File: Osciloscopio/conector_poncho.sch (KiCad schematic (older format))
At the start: 1 part

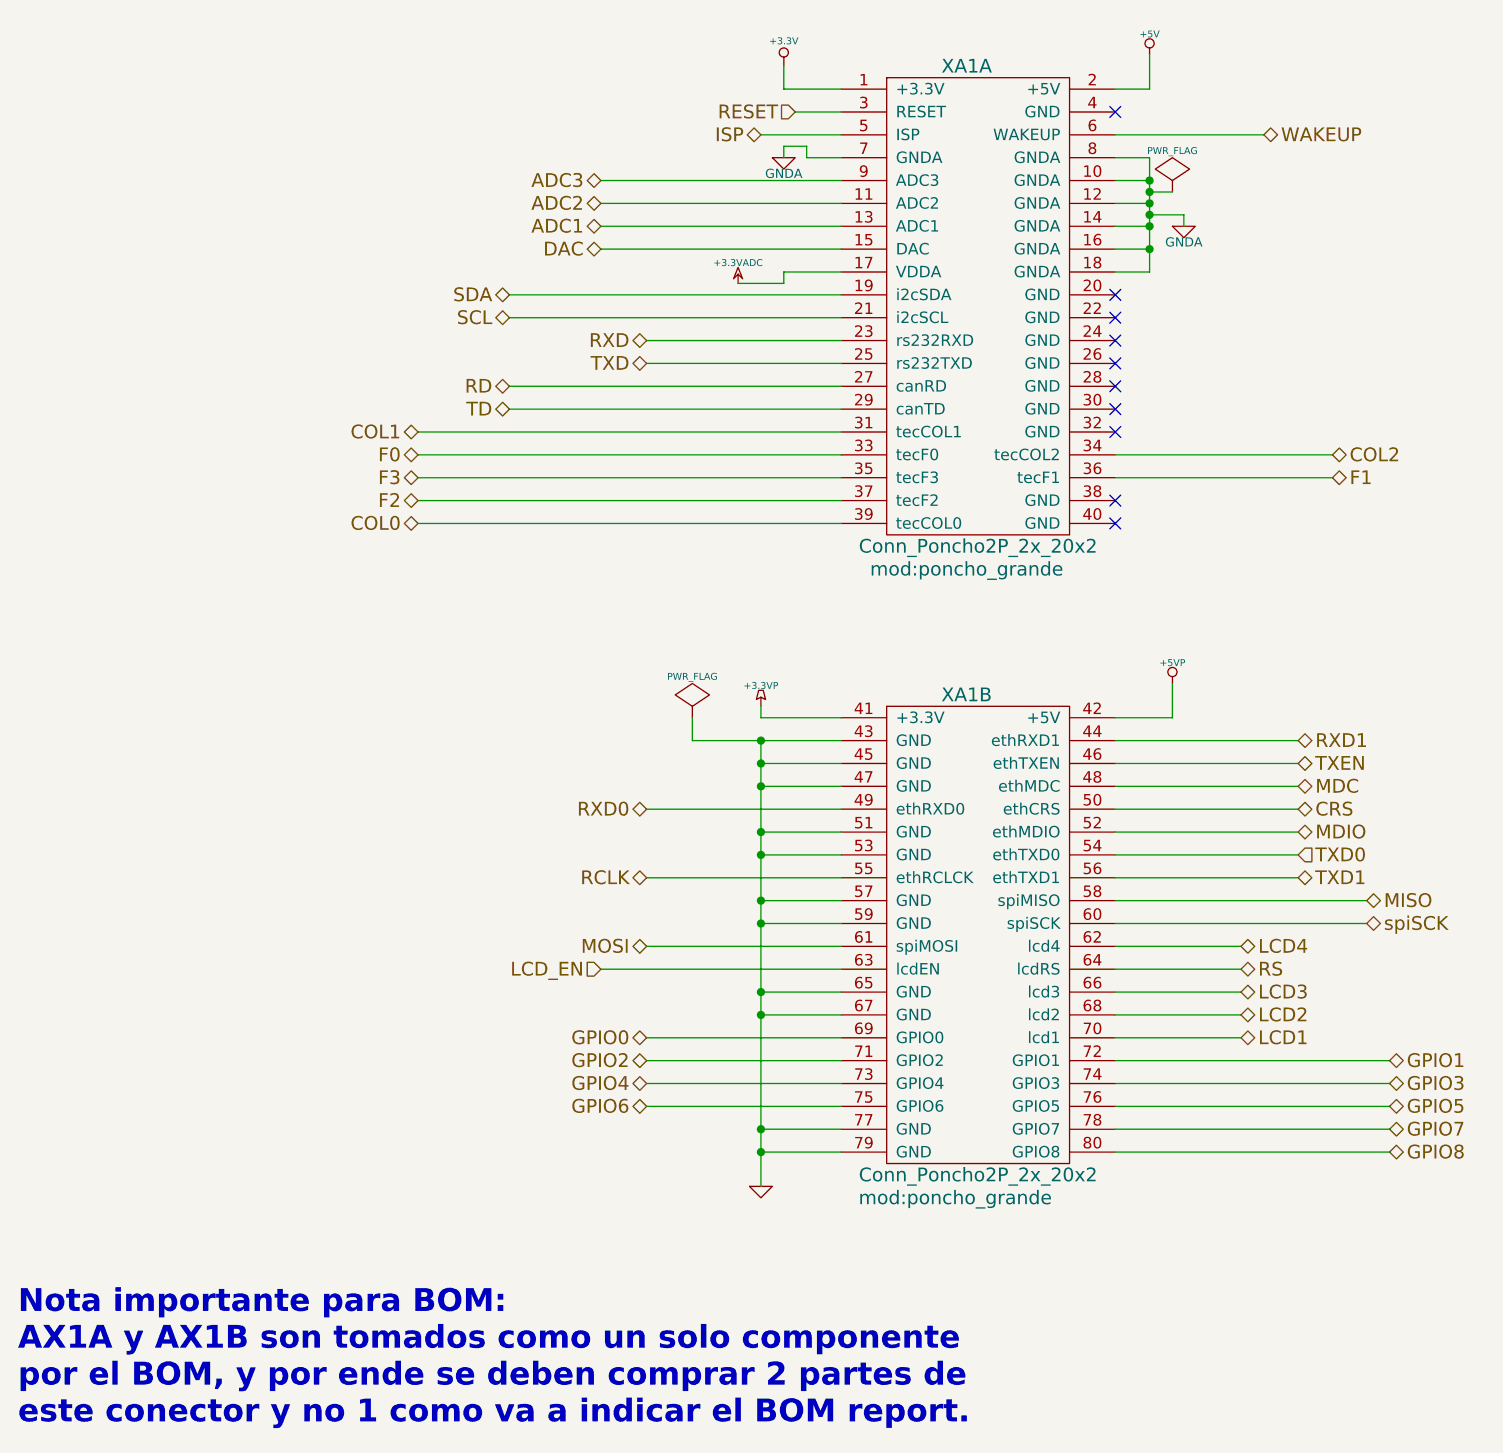
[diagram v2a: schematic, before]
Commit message: Se finalizan las correciones sugeridas a nivel esquematico
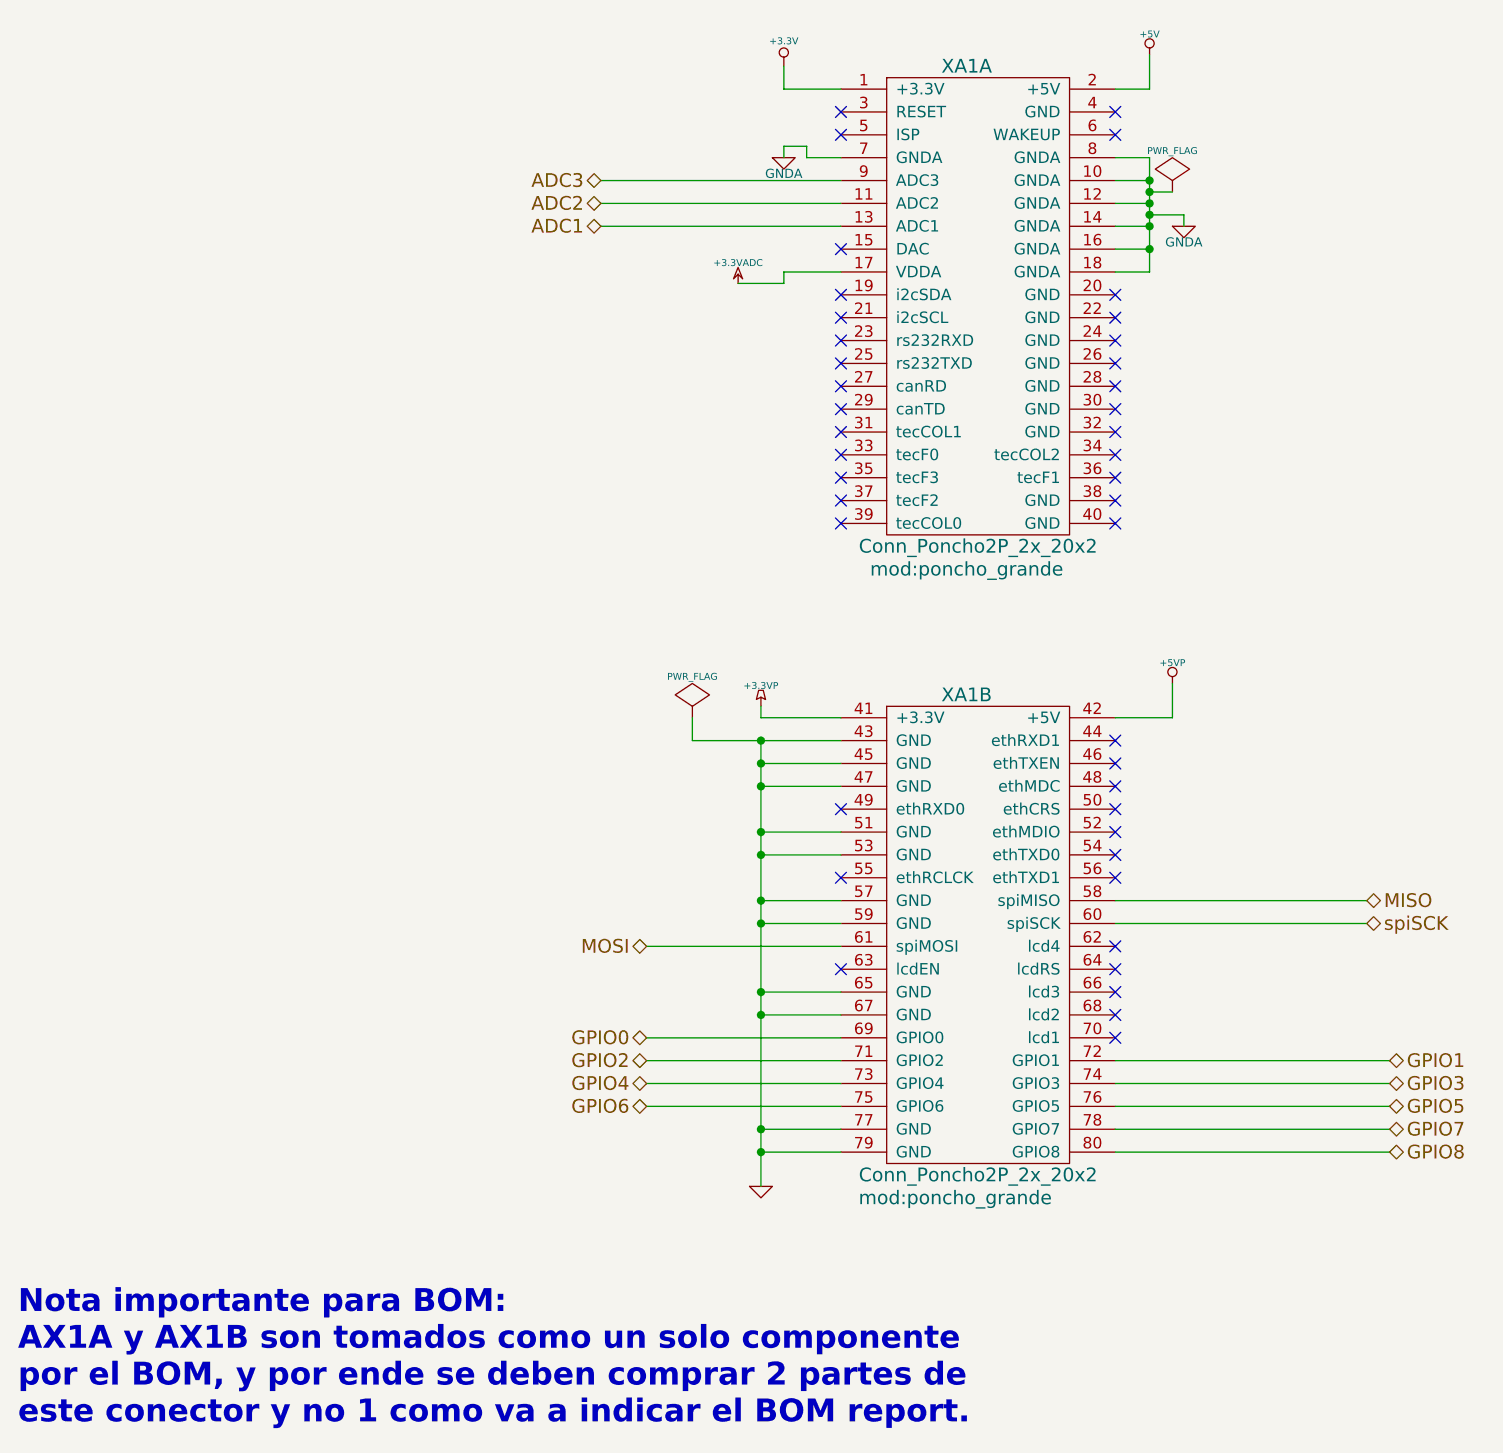
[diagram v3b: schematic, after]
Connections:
- net COL0: no longer names the net of XA1.39 (tecCOL0)
- net COL1: no longer names the net of XA1.31 (tecCOL1)
- net COL2: no longer names the net of XA1.34 (tecCOL2)
- net CRS: no longer names the net of XA1.50 (ethCRS)
- net DAC: no longer names the net of XA1.15 (DAC)
- net F0: no longer names the net of XA1.33 (tecF0)
- net F1: no longer names the net of XA1.36 (tecF1)
- net F2: no longer names the net of XA1.37 (tecF2)
- net F3: no longer names the net of XA1.35 (tecF3)
- net ISP: no longer names the net of XA1.5 (ISP)
- net LCD1: no longer names the net of XA1.70 (lcd1)
- net LCD2: no longer names the net of XA1.68 (lcd2)
- net LCD3: no longer names the net of XA1.66 (lcd3)
- net LCD4: no longer names the net of XA1.62 (lcd4)
- net LCD_EN: no longer names the net of XA1.63 (lcdEN)
- net MDC: no longer names the net of XA1.48 (ethMDC)
- net MDIO: no longer names the net of XA1.52 (ethMDIO)
- net RCLK: no longer names the net of XA1.55 (ethRCLCK)
- net RD: no longer names the net of XA1.27 (canRD)
- net RESET: no longer names the net of XA1.3 (RESET)
- net RS: no longer names the net of XA1.64 (lcdRS)
- net RXD: no longer names the net of XA1.23 (rs232RXD)
- net RXD0: no longer names the net of XA1.49 (ethRXD0)
- net RXD1: no longer names the net of XA1.44 (ethRXD1)
- net SCL: no longer names the net of XA1.21 (i2cSCL)
- net SDA: no longer names the net of XA1.19 (i2cSDA)
- net TD: no longer names the net of XA1.29 (canTD)
- net TXD: no longer names the net of XA1.25 (rs232TXD)
- net TXD0: no longer names the net of XA1.54 (ethTXD0)
- net TXD1: no longer names the net of XA1.56 (ethTXD1)
- net TXEN: no longer names the net of XA1.46 (ethTXEN)
- net WAKEUP: no longer names the net of XA1.6 (WAKEUP)
- no-connect marks 10 -> 42
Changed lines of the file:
@@
 EESchema Schematic File Version 2
-LIBS:Poncho_Esqueleto
-LIBS:Misc_Poncho_Grande
-LIBS:device
-LIBS:texas
 LIBS:osc
-LIBS:power
-LIBS:conn
-LIBS:ej2cese
 LIBS:Oscilloscopio-cache
 EELAYER 25 0
@@
 $Descr A4 11693 8268
 encoding utf-8
-Sheet 6 6
+Sheet 6 5
 Title "Poncho Osciloscopio"
 Date "2015-10-06"
@@
 Wire Wire Line
 	4750 3950 4750 3900
-Text HLabel 4900 1300 0    60   Input ~ 0
-RESET
-Wire Wire Line
-	4900 1300 5100 1300
-Text HLabel 4750 1400 0    60   BiDi ~ 0
-ISP
 Wire Wire Line
 	5100 1600 4050 1600
@@
 	5100 1800 4050 1800
 Wire Wire Line
-	5100 1900 4050 1900
-Wire Wire Line
 	4850 2000 5100 2000
-Wire Wire Line
-	5100 2100 3650 2100
-Wire Wire Line
-	5100 2200 3650 2200
-Wire Wire Line
-	5100 2300 4250 2300
-Wire Wire Line
-	5100 2500 3650 2500
-Wire Wire Line
-	5100 2600 3650 2600
-Wire Wire Line
-	5100 2700 3250 2700
-Wire Wire Line
-	5100 2800 3250 2800
-Wire Wire Line
-	5100 2900 3250 2900
-Wire Wire Line
-	5100 3000 3250 3000
-Wire Wire Line
-	5100 3100 3250 3100
 $Comp
 L GNDA #PWR030
@@
 	1    0    0    -1
 $EndComp
-Wire Wire Line
-	5100 1400 4750 1400
 Text HLabel 4050 1600 0    60   BiDi ~ 0
 ADC3
@@
 Text HLabel 4050 1800 0    60   BiDi ~ 0
 ADC1
-Text HLabel 4050 1900 0    60   BiDi ~ 0
-DAC
 $Comp
 L +3.3VADC #PWR031
@@
 Wire Wire Line
 	4950 1450 4950 1500
-Text HLabel 3650 2100 0    60   BiDi ~ 0
-SDA
-Text HLabel 3650 2200 0    60   BiDi ~ 0
-SCL
-Text HLabel 4250 2300 0    60   BiDi ~ 0
-RXD
-Text HLabel 4250 2400 0    60   BiDi ~ 0
-TXD
-Wire Wire Line
-	4250 2400 5100 2400
-Text HLabel 3650 2500 0    60   BiDi ~ 0
-RD
-Text HLabel 3650 2600 0    60   BiDi ~ 0
-TD
-Text HLabel 3250 2700 0    60   BiDi ~ 0
-COL1
-Text HLabel 3250 2800 0    60   BiDi ~ 0
-F0
-Text HLabel 3250 2900 0    60   BiDi ~ 0
-F3
-Text HLabel 3250 3000 0    60   BiDi ~ 0
-F2
-Text HLabel 3250 3100 0    60   BiDi ~ 0
-COL0
-Text HLabel 7250 2800 2    60   BiDi ~ 0
-COL2
-Text HLabel 7250 2900 2    60   BiDi ~ 0
-F1
-Wire Wire Line
-	7250 2800 6300 2800
-Wire Wire Line
-	6300 2900 7250 2900
-Wire Wire Line
-	5100 4350 4250 4350
-Wire Wire Line
-	4250 4650 5100 4650
 Wire Wire Line
 	5100 4950 4250 4950
 Wire Wire Line
-	5100 5050 4050 5050
-Wire Wire Line
 	4250 5350 5100 5350
 Wire Wire Line
@@
 	5100 5650 4250 5650
 Wire Wire Line
-	6300 4050 7100 4050
-Wire Wire Line
-	6300 4150 7100 4150
-Wire Wire Line
-	6300 4250 7100 4250
-Wire Wire Line
-	6300 4350 7100 4350
-Wire Wire Line
-	6300 4450 7100 4450
-Wire Wire Line
-	6300 4550 7100 4550
-Wire Wire Line
-	6300 4650 7100 4650
-Wire Wire Line
 	6300 4750 7400 4750
 Wire Wire Line
 	6300 4850 7400 4850
 Wire Wire Line
-	6300 4950 6850 4950
-Wire Wire Line
-	6300 5050 6850 5050
-Wire Wire Line
-	6300 5150 6850 5150
-Wire Wire Line
-	6300 5250 6850 5250
-Wire Wire Line
-	6300 5350 6850 5350
-Wire Wire Line
 	6300 5550 7500 5550
 Wire Wire Line
@@
 Wire Wire Line
 	6300 5850 7500 5850
-Text HLabel 4250 4350 0    60   BiDi ~ 0
-RXD0
-Text HLabel 4250 4650 0    60   BiDi ~ 0
-RCLK
 Text HLabel 4250 4950 0    60   BiDi ~ 0
 MOSI
-Text HLabel 4050 5050 0    60   Input ~ 0
-LCD_EN
 Text HLabel 4250 5350 0    60   BiDi ~ 0
 GPIO0
@@
 Text HLabel 4250 5650 0    60   BiDi ~ 0
 GPIO6
-Text HLabel 7100 4050 2    60   BiDi ~ 0
-RXD1
-Text HLabel 7100 4150 2    60   BiDi ~ 0
-TXEN
-Text HLabel 7100 4250 2    60   BiDi ~ 0
-MDC
-Text HLabel 7100 4350 2    60   BiDi ~ 0
-CRS
-Text HLabel 7100 4450 2    60   BiDi ~ 0
-MDIO
-Text HLabel 7100 4550 2    60   Input ~ 0
-TXD0
-Text HLabel 7100 4650 2    60   BiDi ~ 0
-TXD1
 Text HLabel 7400 4750 2    60   BiDi ~ 0
 MISO
 Text HLabel 7400 4850 2    60   BiDi ~ 0
 spiSCK
-Text HLabel 6850 4950 2    60   BiDi ~ 0
-LCD4
-Text HLabel 6850 5050 2    60   BiDi ~ 0
-RS
-Text HLabel 6850 5150 2    60   BiDi ~ 0
-LCD3
-Text HLabel 6850 5250 2    60   BiDi ~ 0
-LCD2
-Text HLabel 6850 5350 2    60   BiDi ~ 0
-LCD1
 Text HLabel 7500 5450 2    60   BiDi ~ 0
 GPIO1
@@
 Text HLabel 7500 5850 2    60   BiDi ~ 0
 GPIO8
-Wire Wire Line
-	6300 1400 6950 1400
-Text HLabel 6950 1400 2    60   BiDi ~ 0
-WAKEUP
 $Comp
 L PWR_FLAG #FLG032
@@
 NoConn ~ 6300 3100
 NoConn ~ 6300 1300
+NoConn ~ 5100 1300
+NoConn ~ 5100 1400
+NoConn ~ 5100 1900
+NoConn ~ 5100 2100
+NoConn ~ 5100 2200
+NoConn ~ 5100 2300
+NoConn ~ 5100 2400
+NoConn ~ 5100 2500
+NoConn ~ 5100 2600
+NoConn ~ 5100 2700
+NoConn ~ 5100 2800
+NoConn ~ 5100 2900
+NoConn ~ 5100 3000
+NoConn ~ 5100 3100
+NoConn ~ 6300 2800
+NoConn ~ 6300 2900
+NoConn ~ 6300 1400
+NoConn ~ 5100 4350
+NoConn ~ 5100 4650
+NoConn ~ 6300 4050
+NoConn ~ 6300 4150
+NoConn ~ 6300 4250
+NoConn ~ 6300 4350
+NoConn ~ 6300 4450
+NoConn ~ 6300 4550
+NoConn ~ 6300 4650
+NoConn ~ 6300 4950
+NoConn ~ 6300 5050
+NoConn ~ 6300 5150
+NoConn ~ 6300 5250
+NoConn ~ 6300 5350
+NoConn ~ 5100 5050
 $EndSCHEMATC

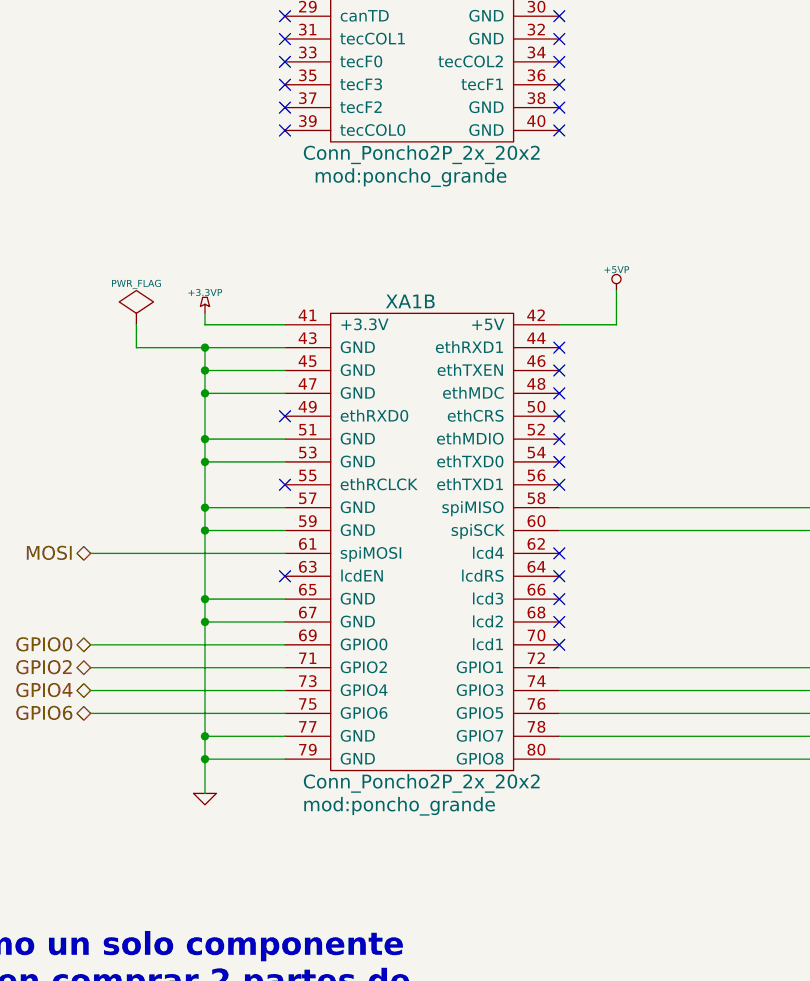
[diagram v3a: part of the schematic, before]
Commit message: Ultimas correciones de la revisión
_ Se copian localmente footprints y se los linkead
_ Se copian localmente los modelos 3D y se los linkea
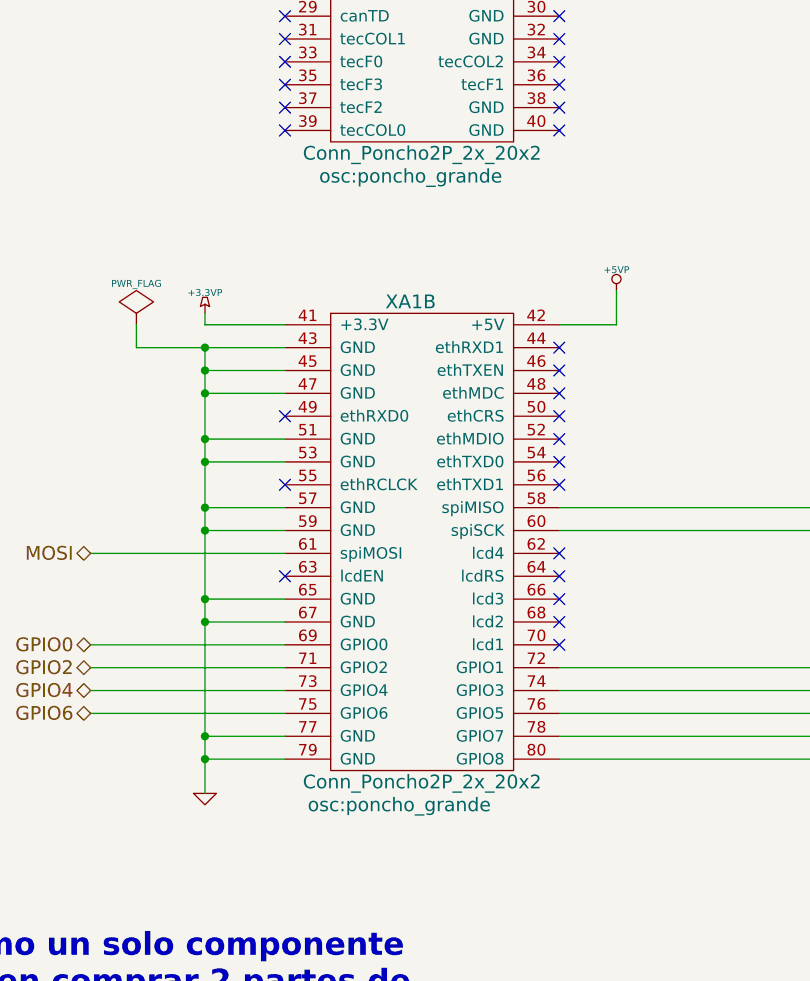
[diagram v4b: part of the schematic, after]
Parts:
- XA1: footprint mod:poncho_grande -> osc:poncho_grande
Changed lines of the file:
@@
 F 0 "XA1" H 5650 4650 60  0000 C CNN
 F 1 "Conn_Poncho2P_2x_20x2" H 5700 2550 60  0000 C CNN
-F 2 "mod:poncho_grande" H 5600 2450 60  0000 C CNN
+F 2 "osc:poncho_grande" H 5600 2450 60  0000 C CNN
 F 3 "" H 5350 4250 60  0000 C CNN
 F 4 "S6104-ND" H 5350 4250 60  0001 C CNN "Digikey#"
@@
 F 0 "XA1" H 5650 1900 60  0000 C CNN
 F 1 "Conn_Poncho2P_2x_20x2" H 5700 -200 60  0000 C CNN
-F 2 "mod:poncho_grande" H 5650 -300 60  0000 C CNN
+F 2 "osc:poncho_grande" H 5650 -300 60  0000 C CNN
 F 3 "" H 5350 1500 60  0000 C CNN
 F 4 "S6104-ND" H 5350 1500 60  0001 C CNN "Digikey#"

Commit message: Corrección cod. digikey del conector de poncho osciloscopio, aclaración sobre zócalos para los dip.
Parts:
- XA1: Digikey# S6104-ND -> S2012E-20-ND; Manf# PPTC202LFBN-RC -> PEC20DAAN
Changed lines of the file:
@@
 $Descr A4 11693 8268
 encoding utf-8
-Sheet 6 5
+Sheet 5 5
 Title "Poncho Osciloscopio"
 Date "2015-10-06"
@@
 F 2 "osc:poncho_grande" H 5600 2450 60  0000 C CNN
 F 3 "" H 5350 4250 60  0000 C CNN
-F 4 "S6104-ND" H 5350 4250 60  0001 C CNN "Digikey#"
-F 5 "PPTC202LFBN-RC" H 5350 4250 60  0001 C CNN "Manf#"
-F 6 "Sullins Connector Solutions" H 5350 4250 60  0001 C CNN "Manf"
+F 4 "Sullins Connector Solutions" H 5350 4250 60  0001 C CNN "Manf"
+F 5 "PEC20DAAN" H 5350 4250 60  0001 C CNN "Manf#"
+F 6 "S2012E-20-ND" H 5350 4250 60  0001 C CNN "Digikey#"
 	2    5350 4250
 	1    0    0    -1
@@
 F 2 "osc:poncho_grande" H 5650 -300 60  0000 C CNN
 F 3 "" H 5350 1500 60  0000 C CNN
-F 4 "S6104-ND" H 5350 1500 60  0001 C CNN "Digikey#"
-F 5 "PPTC202LFBN-RC" H 5350 1500 60  0001 C CNN "Manf#"
-F 6 "Sullins Connector Solutions" H 5350 1500 60  0001 C CNN "Manf"
+F 4 "Sullins Connector Solutions" H 5350 1500 60  0001 C CNN "Manf"
+F 5 "PEC20DAAN" H 5350 1500 60  0001 C CNN "Manf#"
+F 6 "S2012E-20-ND" H 5350 1500 60  0001 C CNN "Digikey#"
 	1    5350 1500
 	1    0    0    -1
